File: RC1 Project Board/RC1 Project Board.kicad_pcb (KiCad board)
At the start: 2 copper layers, 99.1 x 99.1 mm, 20 parts, among them J1 Signals, J3 SBC, J4 ADDRESS, J5 Port A, J6 Port B, J7 PWR1, J8 PWR2, M1 Mounting, M2 Mounting, M3 Mounting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

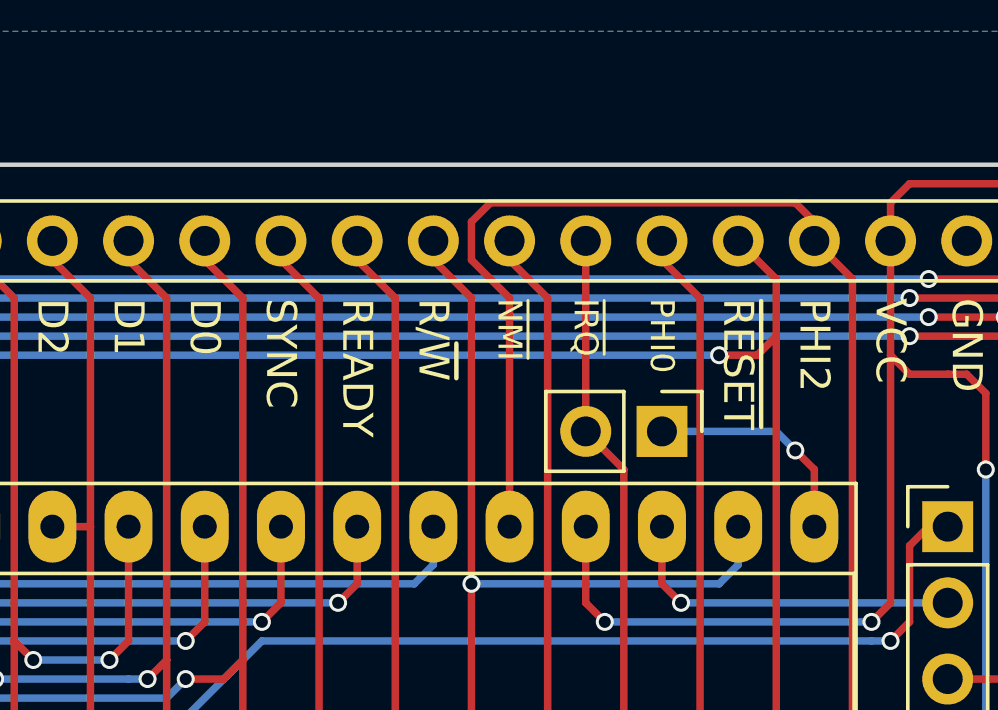
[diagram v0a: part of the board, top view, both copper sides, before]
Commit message: Project board has clock select pins
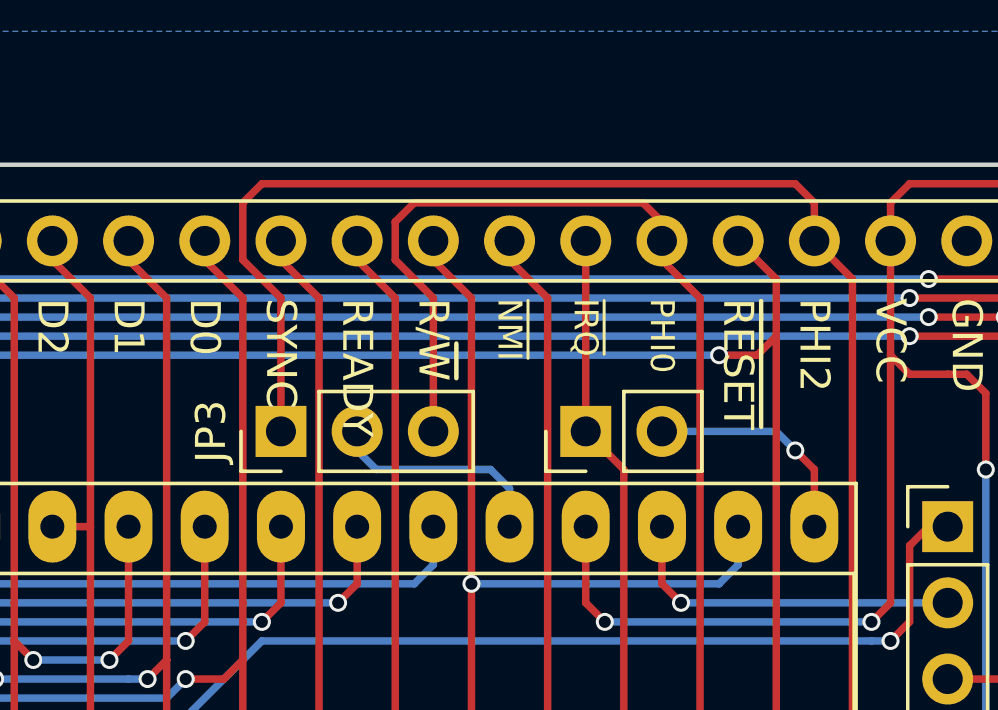
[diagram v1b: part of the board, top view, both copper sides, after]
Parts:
- added JP3: VIA_CLK, Pin_Headers:Pin_Header_Straight_1x03_Pitch2.54mm, F.Cu at (134.6, 57.1)
- moved JP1 2.54 mm to (144.8, 57.1), turned to 90 degrees
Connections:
- JP1 pad 1: Net-(JP1-Pad1) -> /~IRQ
- JP1 pad 2: /~IRQ -> Net-(JP1-Pad2)
- U2 pad 21: Net-(JP1-Pad1) -> Net-(JP1-Pad2)
- U2 pad 25: /PHI2 -> Net-(JP3-Pad2)
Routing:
- net /PHI0: track 96.7 -> 114.3 mm
- net Net-(JP1-Pad2): track 0.00 -> 7.51 mm, vias 0 -> 1
- net Net-(JP1-Pad1): track 7.51 -> 0.00 mm, vias 1 -> 0
- net Net-(JP3-Pad2): track 0.00 -> 7.51 mm
- net /PHI2: track 120.0 -> 125.7 mm
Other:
- board text added: "VIA_CLK"
- board text added: "VIA_IRQ"
- board text removed: "LINK IRQ TO BUS"
